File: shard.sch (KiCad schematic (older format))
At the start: 52 parts, among them J1 Audio-Jack-4, U1 ARDUINO_PRO_MICRO

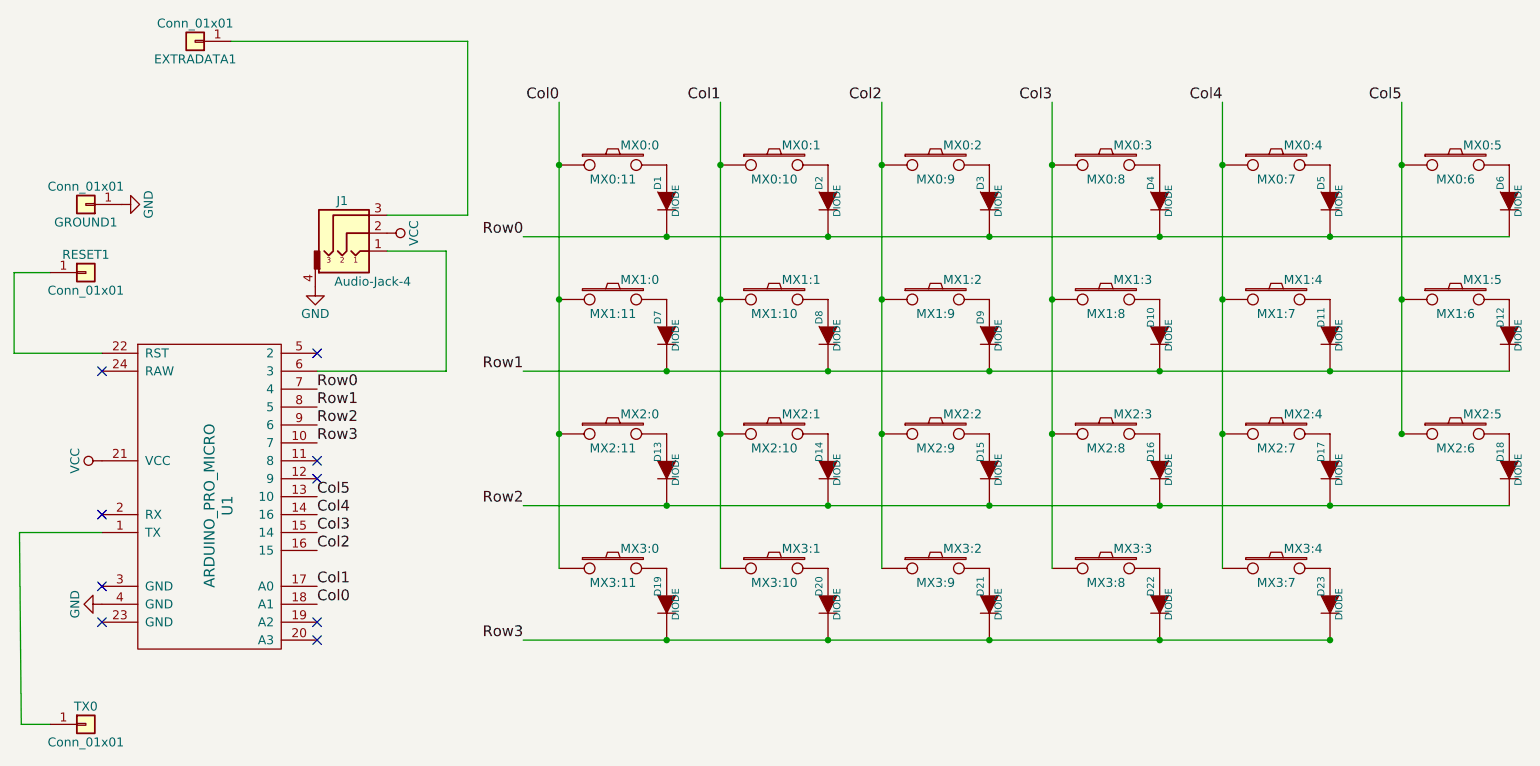
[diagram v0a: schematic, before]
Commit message: Add holes for standoffs and re-route
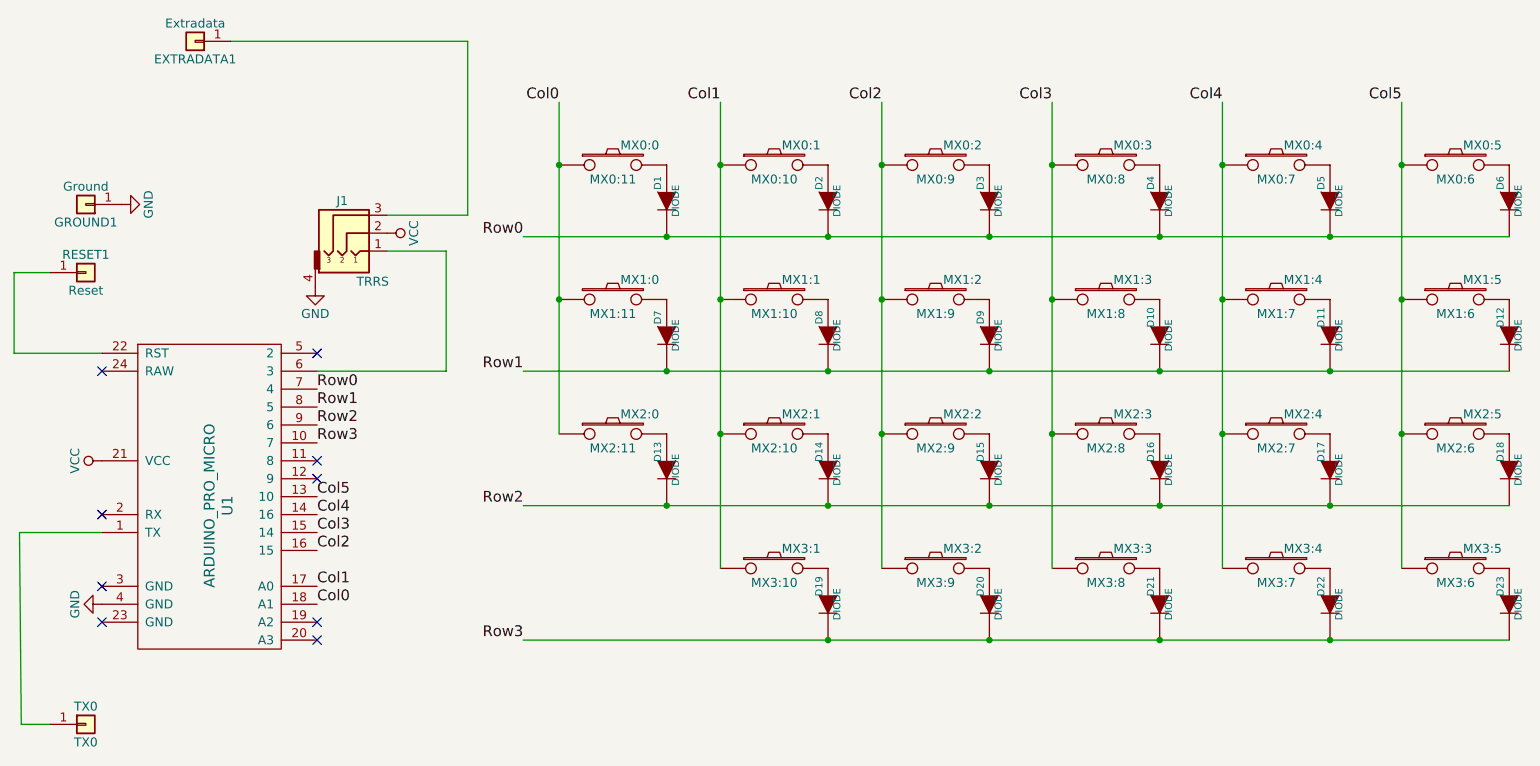
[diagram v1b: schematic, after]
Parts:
- EXTRADATA1: value Conn_01x01 -> Extradata
- GROUND1: value Conn_01x01 -> Ground
- J1: value Audio-Jack-4 -> TRRS
- MX3:1: renamed from MX3:0; value MX3:11 -> MX3:10
- MX3:2: renamed from MX3:1; value MX3:10 -> MX3:9
- MX3:3: renamed from MX3:2; value MX3:9 -> MX3:8
- MX3:4: renamed from MX3:3; value MX3:8 -> MX3:7
- MX3:5: renamed from MX3:4; value MX3:7 -> MX3:6
- RESET1: value Conn_01x01 -> Reset
- TX0: value Conn_01x01 -> TX0
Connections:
- net Col0: no longer MX3:1.1
- net Col1: now also MX3:1.1; no longer MX3:2.1
- net Col2: now also MX3:2.1; no longer MX3:3.1
- net Col3: now also MX3:3.1; no longer MX3:4.1
- net Col4: now also MX3:4.1; no longer MX3:5.1
- net Col5: now also MX3:5.1
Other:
- moved on the sheet: D19, D20, D21, D22, D23, MX3:1, MX3:2, MX3:3, MX3:4, MX3:5
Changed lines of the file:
@@
 	0    1    1    0
 $EndComp
-Wire Wire Line
-	3450 3000 8950 3000
-Connection ~ 7950 3000
-Connection ~ 6050 3000
-Connection ~ 7000 3000
-Connection ~ 5150 3000
 $Comp
 L SWITCH_PUSH MX0:0
@@
 	0    1    1    0
 $EndComp
-Wire Wire Line
-	3450 2250 8950 2250
-Connection ~ 7950 2250
-Connection ~ 6050 2250
-Connection ~ 7000 2250
-Connection ~ 5150 2250
 $Comp
 L SWITCH_PUSH MX2:0
@@
 	0    1    1    0
 $EndComp
-Wire Wire Line
-	3450 3750 8950 3750
-Connection ~ 7950 3750
-Connection ~ 6050 3750
-Connection ~ 7000 3750
-Connection ~ 5150 3750
-$Comp
-L SWITCH_PUSH MX3:0
+$Comp
+L SWITCH_PUSH MX3:1
 U 1 1 59F66261
-P 3950 4100
-F 0 "MX3:0" H 4100 4210 50  0000 C CNN
-F 1 "MX3:11" H 3950 4020 50  0000 C CNN
-F 2 "Keyboard:MX_DoubleSided" H 3950 4100 60  0001 C CNN
-F 3 "" H 3950 4100 60  0000 C CNN
-	1    3950 4100
-	1    0    0    -1
-$EndComp
-$Comp
-L DIODE D19
-U 1 1 59F66268
-P 4250 4300
-F 0 "D19" H 4150 4250 40  0000 C CNN
-F 1 "DIODE" H 4250 4350 40  0000 C CNN
-F 2 "keyboard_parts:D_SOD123_axial" H 4250 4300 60  0001 C CNN
-F 3 "" H 4250 4300 60  0001 C CNN
-	1    4250 4300
-	0    1    1    0
-$EndComp
-$Comp
-L SWITCH_PUSH MX3:1
-U 1 1 59F6626F
 P 4850 4100
 F 0 "MX3:1" H 5000 4210 50  0000 C CNN
@@
 $EndComp
 $Comp
-L DIODE D20
-U 1 1 59F66276
+L DIODE D19
+U 1 1 59F66268
 P 5150 4300
-F 0 "D20" H 5050 4250 40  0000 C CNN
+F 0 "D19" H 5050 4250 40  0000 C CNN
 F 1 "DIODE" H 5150 4350 40  0000 C CNN
 F 2 "keyboard_parts:D_SOD123_axial" H 5150 4300 60  0001 C CNN
@@
 $Comp
 L SWITCH_PUSH MX3:2
-U 1 1 59F6627D
+U 1 1 59F6626F
 P 5750 4100
 F 0 "MX3:2" H 5900 4210 50  0000 C CNN
@@
 $EndComp
 $Comp
+L DIODE D20
+U 1 1 59F66276
+P 6050 4300
+F 0 "D20" H 5950 4250 40  0000 C CNN
+F 1 "DIODE" H 6050 4350 40  0000 C CNN
+F 2 "keyboard_parts:D_SOD123_axial" H 6050 4300 60  0001 C CNN
+F 3 "" H 6050 4300 60  0001 C CNN
+	1    6050 4300
+	0    1    1    0
+$EndComp
+$Comp
 L SWITCH_PUSH MX3:3
-U 1 1 59F66284
+U 1 1 59F6627D
 P 6700 4100
 F 0 "MX3:3" H 6850 4210 50  0000 C CNN
@@
 $Comp
 L SWITCH_PUSH MX3:4
-U 1 1 59F6628B
+U 1 1 59F66284
 P 7650 4100
 F 0 "MX3:4" H 7800 4210 50  0000 C CNN
@@
 $EndComp
 $Comp
+L SWITCH_PUSH MX3:5
+U 1 1 59F6628B
+P 8650 4100
+F 0 "MX3:5" H 8800 4210 50  0000 C CNN
+F 1 "MX3:6" H 8650 4020 50  0000 C CNN
+F 2 "Keyboard:MX_DoubleSided" H 8650 4100 60  0001 C CNN
+F 3 "" H 8650 4100 60  0000 C CNN
+	1    8650 4100
+	1    0    0    -1
+$EndComp
+$Comp
 L DIODE D21
 U 1 1 59F66299
-P 6050 4300
-F 0 "D21" H 5950 4250 40  0000 C CNN
-F 1 "DIODE" H 6050 4350 40  0000 C CNN
-F 2 "keyboard_parts:D_SOD123_axial" H 6050 4300 60  0001 C CNN
-F 3 "" H 6050 4300 60  0001 C CNN
-	1    6050 4300
-	0    1    1    0
-$EndComp
-$Comp
-L DIODE D22
-U 1 1 59F662A0
 P 7000 4300
-F 0 "D22" H 6900 4250 40  0000 C CNN
+F 0 "D21" H 6900 4250 40  0000 C CNN
 F 1 "DIODE" H 7000 4350 40  0000 C CNN
 F 2 "keyboard_parts:D_SOD123_axial" H 7000 4300 60  0001 C CNN
@@
 $EndComp
 $Comp
-L DIODE D23
-U 1 1 59F662A7
+L DIODE D22
+U 1 1 59F662A0
 P 7950 4300
-F 0 "D23" H 7850 4250 40  0000 C CNN
+F 0 "D22" H 7850 4250 40  0000 C CNN
 F 1 "DIODE" H 7950 4350 40  0000 C CNN
 F 2 "keyboard_parts:D_SOD123_axial" H 7950 4300 60  0001 C CNN
@@
 	0    1    1    0
 $EndComp
-Wire Wire Line
-	3450 4500 7950 4500
-Connection ~ 7950 4500
-Connection ~ 6050 4500
-Connection ~ 7000 4500
-Connection ~ 5150 4500
-Wire Wire Line
-	3650 1500 3650 4100
-Connection ~ 3650 2600
-Connection ~ 3650 3350
-Wire Wire Line
-	4550 1500 4550 4100
-Connection ~ 4550 3350
-Wire Wire Line
-	5450 1500 5450 4100
-Connection ~ 5450 3350
-Wire Wire Line
-	6400 1500 6400 4100
-Connection ~ 6400 3350
-Wire Wire Line
-	7350 1500 7350 4100
-Connection ~ 7350 3350
-Wire Wire Line
-	8350 1500 8350 3350
-Connection ~ 8350 3350
-Connection ~ 8350 2600
-Connection ~ 7350 2600
-Connection ~ 6400 2600
-Connection ~ 5450 2600
-Connection ~ 4550 2600
+$Comp
+L DIODE D23
+U 1 1 59F662A7
+P 8950 4300
+F 0 "D23" H 8850 4250 40  0000 C CNN
+F 1 "DIODE" H 8950 4350 40  0000 C CNN
+F 2 "keyboard_parts:D_SOD123_axial" H 8950 4300 60  0001 C CNN
+F 3 "" H 8950 4300 60  0001 C CNN
+	1    8950 4300
+	0    1    1    0
+$EndComp
 NoConn ~ 2300 2900
 NoConn ~ 2300 3500
@@
 Text Label 8350 1500 2    60   ~ 0
 Col5
-Connection ~ 3650 1850
-Connection ~ 4550 1850
-Connection ~ 5450 1850
-Connection ~ 6400 1850
-Connection ~ 7350 1850
-Connection ~ 8350 1850
-Connection ~ 4250 2250
-Connection ~ 4250 3000
-Connection ~ 4250 3750
-Connection ~ 4250 4500
 $Comp
 L GND #PWR03
@@
 P 2490 2130
 F 0 "J1" H 2440 2210 50  0000 C CNN
-F 1 "Audio-Jack-4" H 2610 1760 50  0000 C CNN
+F 1 "TRRS" H 2610 1760 50  0000 C CNN
 F 2 "Keyboard:PJ320A_3.5mm_Jack" H 2740 2230 50  0001 C CNN
 F 3 "" H 2740 2230 50  0001 C CNN
@@
 	1    0    0    -1
 $EndComp
-Wire Wire Line
-	1100 2900 610  2900
-Wire Wire Line
-	610  2900 610  2450
-Wire Wire Line
-	610  2450 810  2450
 $Comp
 L GND #PWR05
@@
 	0    -1   -1   0
 $EndComp
-Wire Wire Line
-	1100 3900 640  3900
-Wire Wire Line
-	640  3900 650  4970
-Wire Wire Line
-	650  4970 810  4970
-Wire Wire Line
-	2690 2130 3140 2130
-Wire Wire Line
-	3140 2130 3140 1160
-Wire Wire Line
-	3140 1160 1820 1160
-Wire Wire Line
-	2300 3000 3020 3000
-Wire Wire Line
-	3020 3000 3020 2330
-Wire Wire Line
-	3020 2330 2690 2330
 $Comp
 L Conn_01x01 TX0
@@
 P 1010 4970
 F 0 "TX0" H 1010 5070 50  0000 C CNN
-F 1 "Conn_01x01" H 1010 4870 50  0000 C CNN
+F 1 "TX0" H 1010 4870 50  0000 C CNN
 F 2 "keyboard_parts:PIN_1_SQUARE" H 1010 4970 50  0001 C CNN
 F 3 "" H 1010 4970 50  0001 C CNN
@@
 P 1620 1160
 F 0 "EXTRADATA1" H 1620 1260 50  0000 C CNN
-F 1 "Conn_01x01" H 1620 1060 50  0000 C CNN
+F 1 "Extradata" H 1620 1060 50  0000 C CNN
 F 2 "keyboard_parts:PIN_1_SQUARE" H 1620 1160 50  0001 C CNN
 F 3 "" H 1620 1160 50  0001 C CNN
@@
 P 1010 2450
 F 0 "RESET1" H 1010 2550 50  0000 C CNN
-F 1 "Conn_01x01" H 1010 2350 50  0000 C CNN
+F 1 "Reset" H 1010 2350 50  0000 C CNN
 F 2 "keyboard_parts:PIN_1_SQUARE" H 1010 2450 50  0001 C CNN
 F 3 "" H 1010 2450 50  0001 C CNN
@@
 P 1010 2070
 F 0 "GROUND1" H 1010 2170 50  0000 C CNN
-F 1 "Conn_01x01" H 1010 1970 50  0000 C CNN
+F 1 "Ground" H 1010 1970 50  0000 C CNN
 F 2 "keyboard_parts:PIN_1_SQUARE" H 1010 2070 50  0001 C CNN
 F 3 "" H 1010 2070 50  0001 C CNN
@@
 NoConn ~ 1100 4200
 NoConn ~ 1100 4400
+Wire Wire Line
+	3020 2330 2690 2330
+Wire Wire Line
+	3020 3000 3020 2330
+Wire Wire Line
+	2300 3000 3020 3000
+Wire Wire Line
+	3140 1160 1820 1160
+Wire Wire Line
+	3140 2130 3140 1160
+Wire Wire Line
+	2690 2130 3140 2130
+Wire Wire Line
+	650  4970 810  4970
+Wire Wire Line
+	640  3900 650  4970
+Wire Wire Line
+	1100 3900 640  3900
+Wire Wire Line
+	610  2450 810  2450
+Wire Wire Line
+	610  2900 610  2450
+Wire Wire Line
+	1100 2900 610  2900
+Connection ~ 4250 3750
+Connection ~ 4250 3000
+Connection ~ 4250 2250
+Connection ~ 8350 1850
+Connection ~ 7350 1850
+Connection ~ 6400 1850
+Connection ~ 5450 1850
+Connection ~ 4550 1850
+Connection ~ 3650 1850
+Connection ~ 4550 2600
+Connection ~ 5450 2600
+Connection ~ 6400 2600
+Connection ~ 7350 2600
+Connection ~ 8350 2600
+Connection ~ 8350 3350
+Wire Wire Line
+	8350 1500 8350 4100
+Connection ~ 7350 3350
+Wire Wire Line
+	7350 1500 7350 4100
+Connection ~ 6400 3350
+Wire Wire Line
+	6400 1500 6400 4100
+Connection ~ 5450 3350
+Wire Wire Line
+	5450 1500 5450 4100
+Connection ~ 4550 3350
+Wire Wire Line
+	4550 1500 4550 4100
+Connection ~ 3650 2600
+Connection ~ 5150 4500
+Connection ~ 7000 4500
+Connection ~ 6050 4500
+Connection ~ 5150 3750
+Connection ~ 7000 3750
+Connection ~ 6050 3750
+Connection ~ 7950 3750
+Wire Wire Line
+	3450 3750 8950 3750
+Connection ~ 5150 2250
+Connection ~ 7000 2250
+Connection ~ 6050 2250
+Connection ~ 7950 2250
+Wire Wire Line
+	3450 2250 8950 2250
+Connection ~ 5150 3000
+Connection ~ 7000 3000
+Connection ~ 6050 3000
+Connection ~ 7950 3000
+Wire Wire Line
+	3450 3000 8950 3000
+Wire Wire Line
+	3450 4500 8950 4500
+Connection ~ 7950 4500
+Wire Wire Line
+	3650 1500 3650 3350
 $EndSCHEMATC

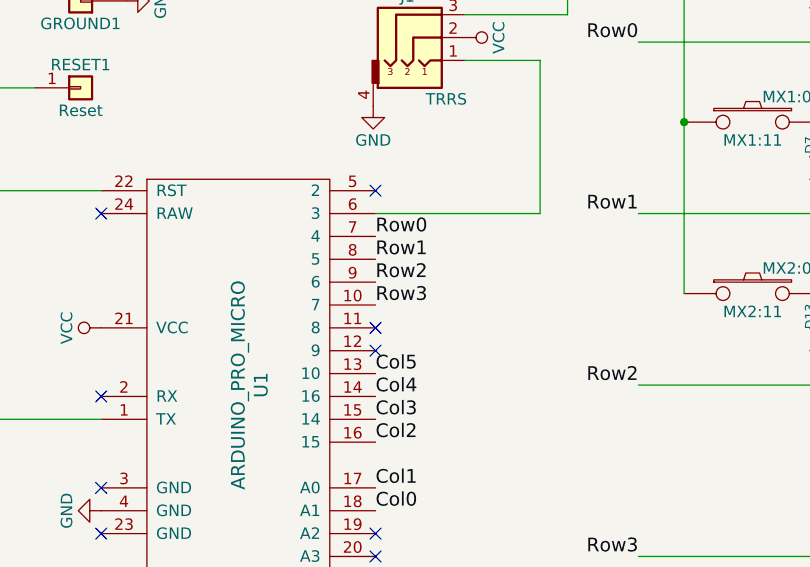
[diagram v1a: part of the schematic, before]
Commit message: Adjust Pro Micro pinout to match Let's Split
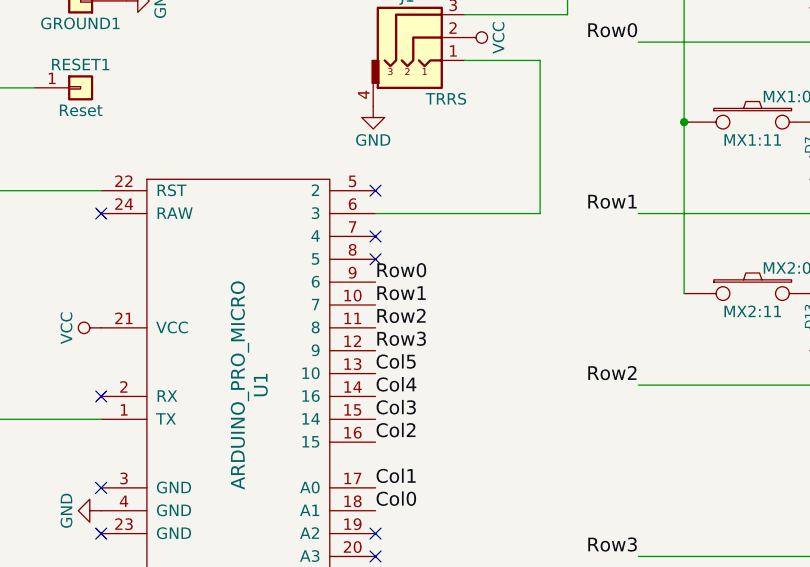
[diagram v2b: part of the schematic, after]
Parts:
- U1: footprint keebs:Pro_Micro -> footprints:ARDUINO_PRO_MICRO
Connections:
- net Row0: now also U1.9 (6); no longer U1.7 (4)
- net Row1: now also U1.10 (7); no longer U1.8 (5)
- net Row2: now also U1.11 (8); no longer U1.9 (6)
- net Row3: now also U1.12 (9); no longer U1.10 (7)
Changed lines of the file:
@@
 F 0 "U1" V 1800 3650 60  0000 C CNN
 F 1 "ARDUINO_PRO_MICRO" V 1700 3650 60  0000 C CNN
-F 2 "keebs:Pro_Micro" H 1550 4200 60  0001 C CNN
+F 2 "footprints:ARDUINO_PRO_MICRO" H 1550 4200 60  0001 C CNN
 F 3 "" H 1550 4200 60  0000 C CNN
 	1    1700 3700
@@
 $EndComp
 NoConn ~ 2300 2900
-NoConn ~ 2300 3500
-NoConn ~ 2300 3600
 NoConn ~ 2300 4400
 NoConn ~ 2300 4500
@@
 Text Label 2300 4200 0    60   ~ 0
 Col1
-Text Label 2300 3100 0    60   ~ 0
+Text Label 2300 3300 0    60   ~ 0
 Row0
-Text Label 2300 3200 0    60   ~ 0
+Text Label 2300 3400 0    60   ~ 0
 Row1
-Text Label 2300 3300 0    60   ~ 0
+Text Label 2300 3500 0    60   ~ 0
 Row2
-Text Label 2300 3400 0    60   ~ 0
+Text Label 2300 3600 0    60   ~ 0
 Row3
 Text Label 2300 4000 0    60   ~ 0
@@
 Wire Wire Line
 	3650 1500 3650 3350
+NoConn ~ 2300 3100
+NoConn ~ 2300 3200
 $EndSCHEMATC
